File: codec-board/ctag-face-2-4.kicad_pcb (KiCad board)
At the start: 4 copper layers, 100 x 100 mm, 245 parts, among them P1001 IO_CONN, P201 PWR5V, U201 MCP1642B, U202 TLV1117, U203 ADP7102, U204 ADP7102, U301 AD1938, U302 ADM811TARTZ, U401 2CH-OPAMP, U402 2CH-OPAMP, U501 2CH-OPAMP, U502 2CH-OPAMP, U601 2CH-OPAMP, U701 2CH-OPAMP, U801 2CH-OPAMP, U901 2CH-OPAMP, Y301 12,288MHz

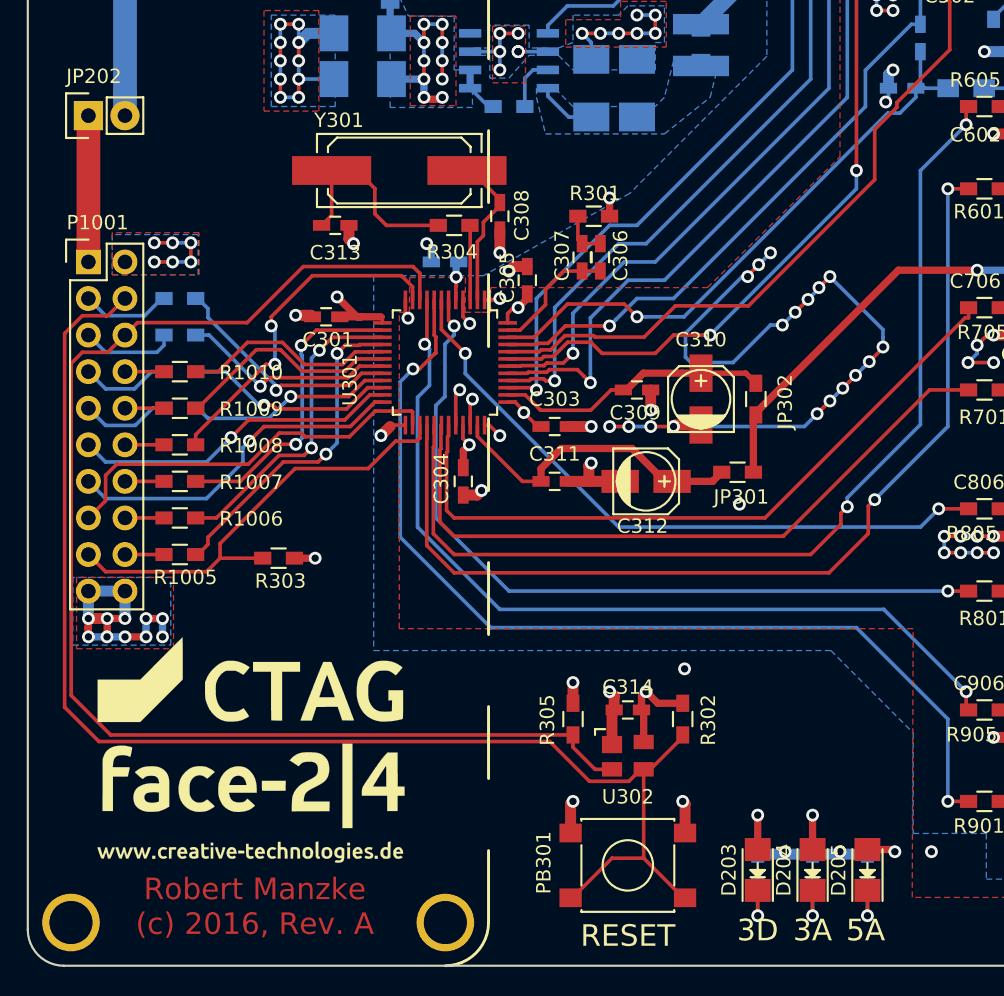
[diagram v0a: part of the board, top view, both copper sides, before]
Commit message: fixed polarity bug on IN2
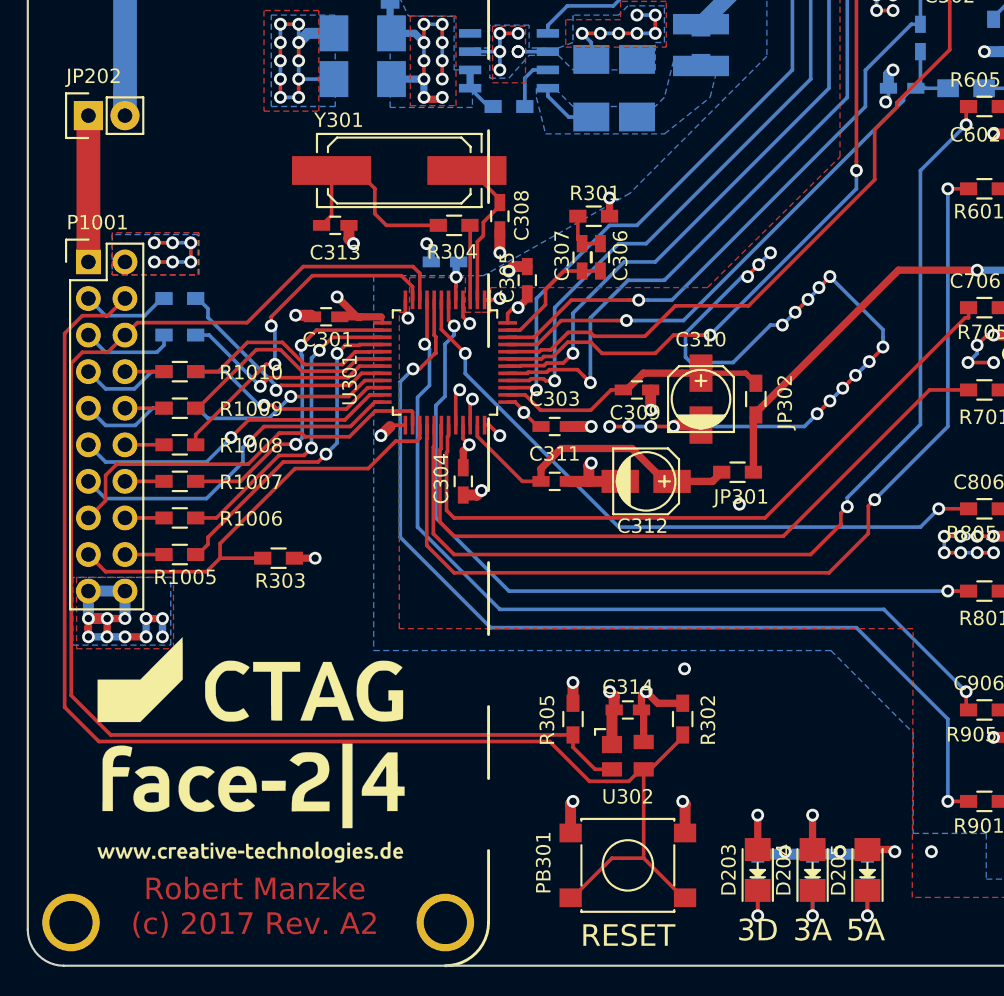
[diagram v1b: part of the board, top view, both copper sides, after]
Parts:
- Y301: value 12,288MHz -> 24,576MHz
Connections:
- net /codec/adc-stereo-buffer-1/ADCLN renamed /codec/adc2
- net /codec/adc-stereo-buffer-1/ADCLP renamed /codec/adc1
- net /codec/adc-stereo-buffer-1/ADCRN renamed /codec/adc4
- net /codec/adc-stereo-buffer-1/ADCRP renamed /codec/adc3
- net /codec/adc-stereo-buffer-2/ADCLN renamed /codec/adc6
- net /codec/adc-stereo-buffer-2/ADCLP renamed /codec/adc5
- net /codec/dac-stereo-buffer-1/LOUTA renamed /codec/dac1
- net /codec/dac-stereo-buffer-1/ROUTA renamed /codec/dac2
- net /codec/dac-stereo-buffer-2/LOUTA renamed /codec/dac3
- net /codec/dac-stereo-buffer-2/ROUTA renamed /codec/dac4
- net /codec/dac-stereo-buffer-3/LOUTA renamed /codec/dac5
- net /codec/dac-stereo-buffer-3/ROUTA renamed /codec/dac6
- net /codec/dac-stereo-buffer-4/LOUTA renamed /codec/dac7
- net /codec/dac-stereo-buffer-4/ROUTA renamed /codec/dac8
- C514 pad 1: /codec/adc-stereo-buffer-2/ADCRN -> /codec/adc8
- C515 pad 1: /codec/adc-stereo-buffer-2/ADCRN -> /codec/adc8
- C515 pad 2: /codec/adc-stereo-buffer-2/ADCRP -> /codec/adc7
- C516 pad 1: /codec/adc-stereo-buffer-2/ADCRP -> /codec/adc7
- C518 pad 1: /codec/adc-stereo-buffer-2/ADCRP -> /codec/adc7
- C519 pad 1: /codec/adc-stereo-buffer-2/ADCRN -> /codec/adc8
- H101 pad 1: Net-(H101-Pad1) -> (no net)
- H102 pad 1: Net-(H102-Pad1) -> (no net)
- H103 pad 1: Net-(H103-Pad1) -> (no net)
- H104 pad 1: Net-(H104-Pad1) -> (no net)
- H105 pad 1: Net-(H105-Pad1) -> (no net)
- H106 pad 1: Net-(H106-Pad1) -> (no net)
- H107 pad 1: Net-(H107-Pad1) -> (no net)
- H108 pad 1: Net-(H108-Pad1) -> (no net)
- U301 pad 45: /codec/adc-stereo-buffer-2/ADCRN -> /codec/adc7
- U301 pad 46: /codec/adc-stereo-buffer-2/ADCRP -> /codec/adc8
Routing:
- net /codec/adc-stereo-buffer-2/ADCRN: track 44.0 -> 0.00 mm, vias 1 -> 0
- net /codec/adc8: track 0.00 -> 43.8 mm, vias 0 -> 1
- net /codec/adc-stereo-buffer-2/ADCRP: track 41.3 -> 0.00 mm, vias 1 -> 0
- net /codec/adc7: track 0.00 -> 40.6 mm, vias 0 -> 1
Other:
- board text added: "Robert Manzke (c) 2017 Rev. A2"
- board text removed: "Robert Manzke (c) 2016, Rev. A"

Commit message: finalized Rev A2
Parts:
- G***: value LOGO-BOX -> LOGO
- moved G*** 4.40 mm to (160.3, 115.4)
- moved G*** 0.77 mm to (127.8, 125.7)
